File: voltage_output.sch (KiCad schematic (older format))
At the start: 29 parts, among them Q1 Q_NPN_BEC

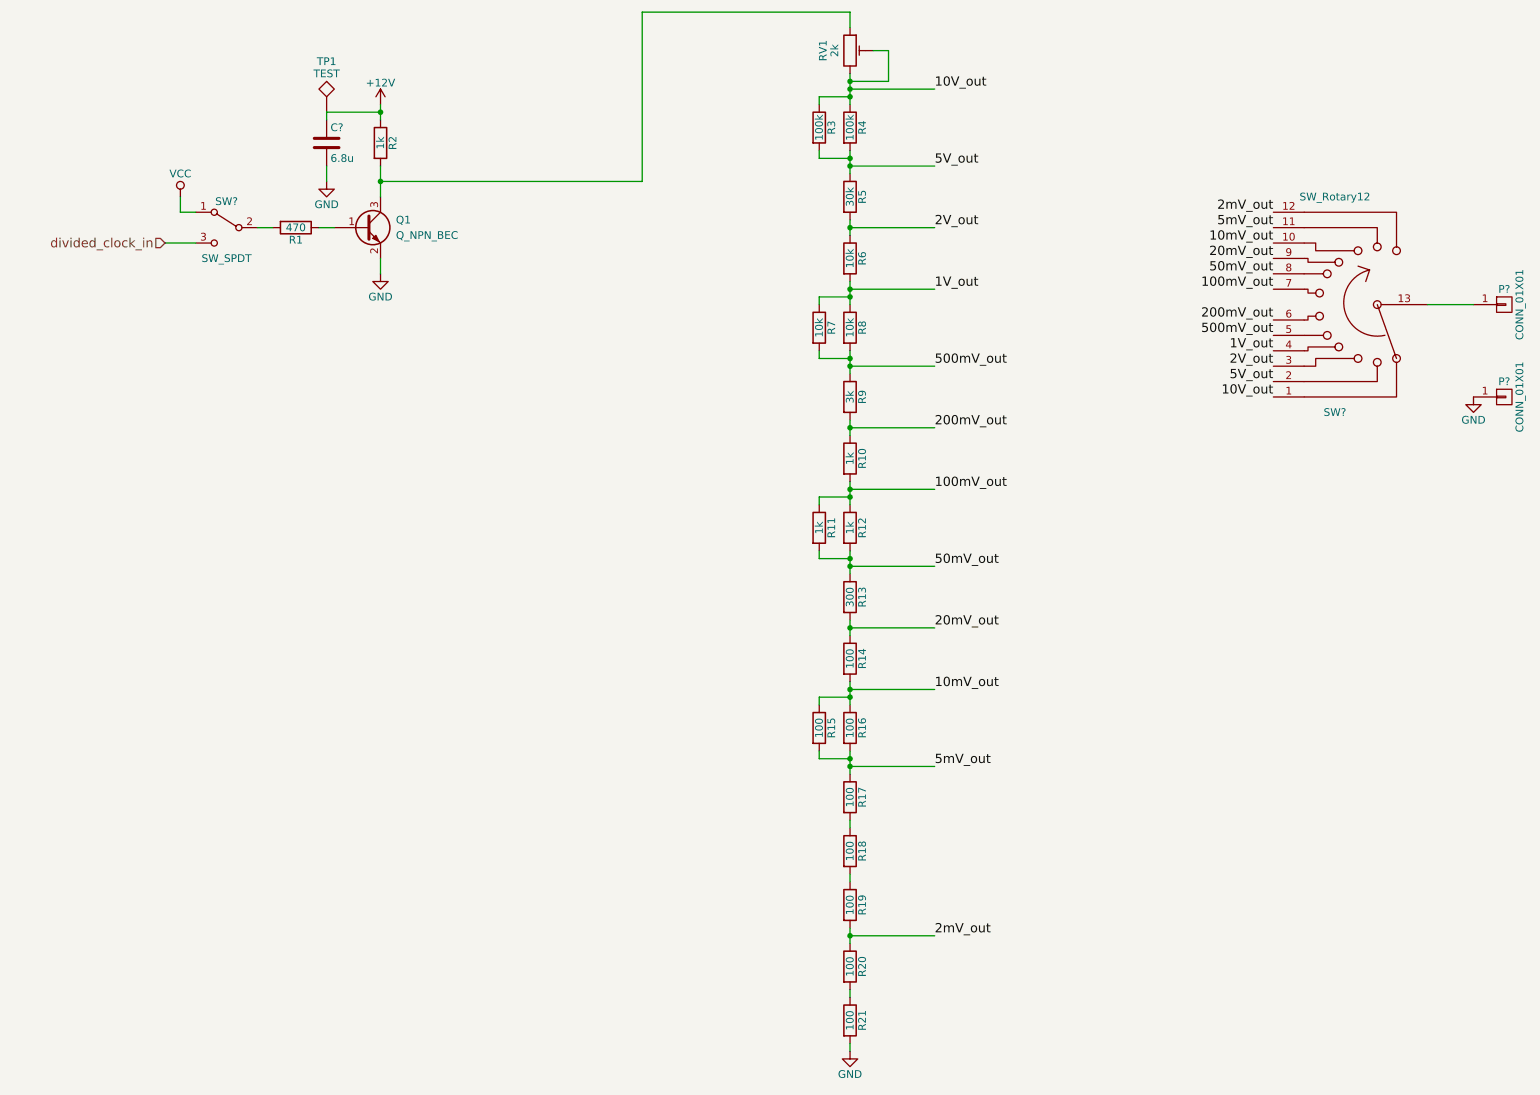
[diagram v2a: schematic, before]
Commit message: R2 PCB rotary switches closer to middle of board
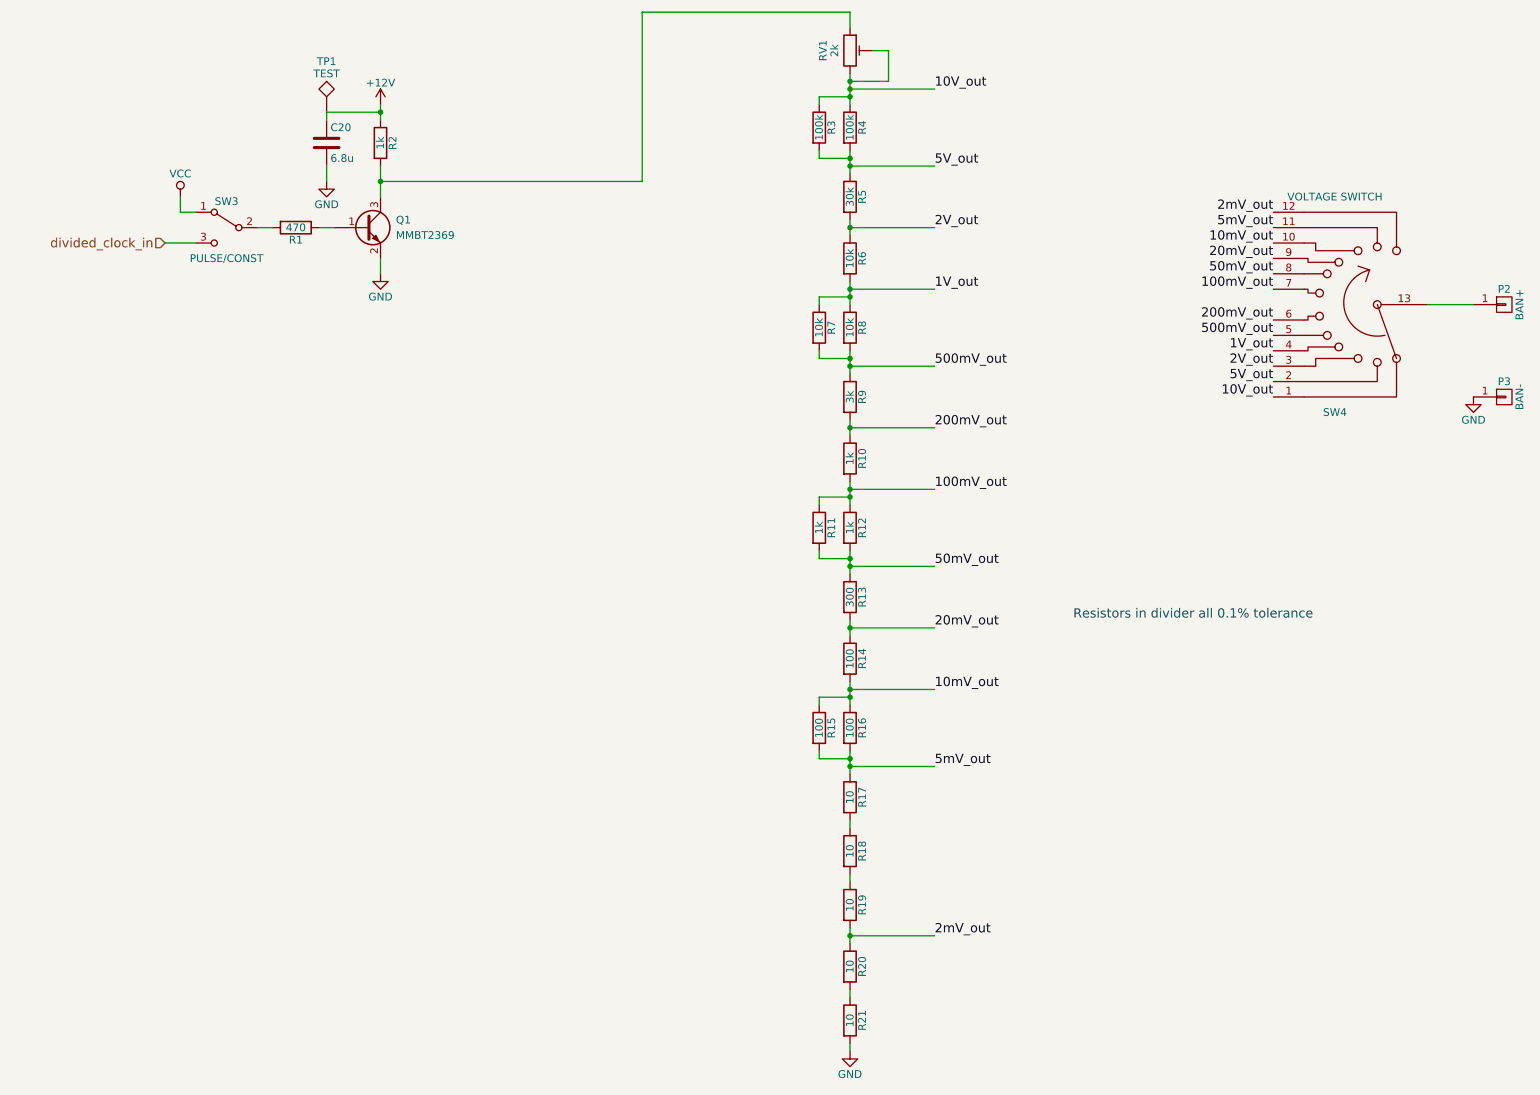
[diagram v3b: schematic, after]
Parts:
- P2: renamed from P?; value CONN_01X01 -> BAN+
- P3: renamed from P?; value CONN_01X01 -> BAN-
- Q1: value Q_NPN_BEC -> MMBT2369; Distributor (none) -> Mouser; Distributor PN (none) -> 863-MMBT2369ALT1G; Manufacturer (none) -> ON Semiconductor; Manufacturer PN (none) -> MMBT2369ALT1G; URL (none) -> http://www.mouser.com/Search/ProductDetail.aspx?R=MMBT2369A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; Unit Price (none) -> 0.19
- R17, R18, R19, R20, R21: value 100 -> 10
- RV1: Distributor (none) -> Mouser; Distributor PN (none) -> 652-3362P-1-202LF; Manufacturer (none) -> Bourns; Manufacturer PN (none) -> 3362P-1-202LF; URL (none) -> http://www.mouser.com/Search/ProductDetail.aspx?R=3362P-1-2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; Unit Price (none) -> 1.02
- SW3: renamed from SW?; value SW_SPDT -> PULSE/CONST; Distributor (none) -> Mouser; Distributor PN (none) -> 633-M201203; Manufacturer (none) -> NKK; Manufacturer PN (none) -> M2012SS1W03; URL (none) -> http://www.mouser.com/Search/ProductDetail.aspx?R=M2012SS1W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; Unit Price (none) -> 2.86
- SW4: renamed from SW?; value SW_Rotary12 -> VOLTAGE SWITCH; Distributor (none) -> Mouser; Distributor PN (none) -> 633-MRK112A; Manufacturer (none) -> NKK; Manufacturer PN (none) -> MRK112-A; URL (none) -> http://www.mouser.com/Search/ProductDetail.aspx?R=MRK112-Av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; Unit Price (none) -> 11.80
- gave numbers to parts that had none: 1
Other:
- note added: "Resistors in divider all 0.1% tolerance"
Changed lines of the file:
@@
 encoding utf-8
 Sheet 5 6
-Title ""
+Title "calbox voltage output"
 Date ""
 Rev ""
@@
 $EndDescr
 $Comp
-L CONN_01X01 P?
+L CONN_01X01 P2
 U 1 1 58C454A6
 P 10000 2500
-F 0 "P?" H 10000 2600 50  0000 C CNN
-F 1 "CONN_01X01" V 10100 2500 50  0000 C CNN
+F 0 "P2" H 10000 2600 50  0000 C CNN
+F 1 "BAN+" V 10100 2500 50  0000 C CNN
 F 2 "Pin_Headers:Pin_Header_Straight_1x01" H 10000 2500 50  0001 C CNN
 F 3 "" H 10000 2500 50  0000 C CNN
@@
 $EndComp
 $Comp
-L CONN_01X01 P?
+L CONN_01X01 P3
 U 1 1 58C454F0
 P 10000 3100
-F 0 "P?" H 10000 3200 50  0000 C CNN
-F 1 "CONN_01X01" V 10100 3100 50  0000 C CNN
+F 0 "P3" H 10000 3200 50  0000 C CNN
+F 1 "BAN-" V 10100 3100 50  0000 C CNN
 F 2 "Pin_Headers:Pin_Header_Straight_1x01" H 10000 3100 50  0001 C CNN
 F 3 "" H 10000 3100 50  0000 C CNN
@@
 P 5750 5700
 F 0 "R17" V 5830 5700 50  0000 C CNN
-F 1 "100" V 5750 5700 50  0000 C CNN
+F 1 "10" V 5750 5700 50  0000 C CNN
 F 2 "Resistors_SMD:R_0805_HandSoldering" V 5680 5700 50  0001 C CNN
 F 3 "" H 5750 5700 50  0000 C CNN
@@
 P 5750 7150
 F 0 "R21" V 5830 7150 50  0000 C CNN
-F 1 "100" V 5750 7150 50  0000 C CNN
+F 1 "10" V 5750 7150 50  0000 C CNN
 F 2 "Resistors_SMD:R_0805_HandSoldering" V 5680 7150 50  0001 C CNN
 F 3 "" H 5750 7150 50  0000 C CNN
@@
 $EndComp
 $Comp
-L GND #PWR67
+L GND #PWR063
 U 1 1 58C45C04
 P 5750 7350
-F 0 "#PWR67" H 5750 7100 50  0001 C CNN
+F 0 "#PWR063" H 5750 7100 50  0001 C CNN
 F 1 "GND" H 5750 7200 50  0000 C CNN
 F 2 "" H 5750 7350 50  0000 C CNN
@@
 $EndComp
 $Comp
-L GND #PWR68
+L GND #PWR064
 U 1 1 58C4A090
 P 9800 3100
-F 0 "#PWR68" H 9800 2850 50  0001 C CNN
+F 0 "#PWR064" H 9800 2850 50  0001 C CNN
 F 1 "GND" H 9800 2950 50  0000 C CNN
 F 2 "" H 9800 3100 50  0000 C CNN
@@
 divided_clock_in
 $Comp
-L SW_SPDT SW?
+L SW_SPDT SW3
 U 1 1 58C4AE53
 P 1700 2000
-F 0 "SW?" H 1700 2170 50  0000 C CNN
-F 1 "SW_SPDT" H 1700 1800 50  0000 C CNN
+F 0 "SW3" H 1700 2170 50  0000 C CNN
+F 1 "PULSE/CONST" H 1700 1800 50  0000 C CNN
 F 2 "calbox:SW_SPDT_NKK_M201xxxx03" H 1700 2000 50  0001 C CNN
-F 3 "" H 1700 2000 50  0000 C CNN
+F 3 "http://www.mouser.com/ds/2/295/MtogglesBushing-31423.pdf" H 1700 2000 50  0001 C CNN
+F 4 "NKK" H 1700 2000 60  0001 C CNN "Manufacturer"
+F 5 "M2012SS1W03" H 1700 2000 60  0001 C CNN "Manufacturer PN"
+F 6 "Mouser" H 1700 2000 60  0001 C CNN "Distributor"
+F 7 "633-M201203" H 1700 2000 60  0001 C CNN "Distributor PN"
+F 8 "http://www.mouser.com/Search/ProductDetail.aspx?R=M2012SS1W03virtualkey63300000virtualkey633-M201203" H 1700 2000 60  0001 C CNN "URL"
+F 9 "2.86" H 1700 2000 60  0001 C CNN "Unit Price"
 	1    1700 2000
 	-1   0    0    -1
@@
 F 1 "2k" V 5650 850 50  0000 C CNN
 F 2 "calbox:Potentiometer_Bourns_3362_ScrewUp" H 5750 850 50  0001 C CNN
-F 3 "" H 5750 850 50  0000 C CNN
+F 3 "http://www.mouser.com/ds/2/54/362-776956.pdf" H 5750 850 50  0001 C CNN
+F 4 "Bourns" V 5750 850 60  0001 C CNN "Manufacturer"
+F 5 "3362P-1-202LF" V 5750 850 60  0001 C CNN "Manufacturer PN"
+F 6 "Mouser" V 5750 850 60  0001 C CNN "Distributor"
+F 7 "652-3362P-1-202LF" V 5750 850 60  0001 C CNN "Distributor PN"
+F 8 "http://www.mouser.com/Search/ProductDetail.aspx?R=3362P-1-202LFvirtualkey65210000virtualkey652-3362P-1-202LF" V 5750 850 60  0001 C CNN "URL"
+F 9 "1.02" V 5750 850 60  0001 C CNN "Unit Price"
 	1    5750 850
 	1    0    0    -1
 $EndComp
 $Comp
-L SW_Rotary12 SW?
+L SW_Rotary12 SW4
 U 1 1 58C77F96
 P 8900 2500
-F 0 "SW?" H 8900 3200 50  0000 C CNN
-F 1 "SW_Rotary12" H 8900 1800 50  0000 C CNN
+F 0 "SW4" H 8900 3200 50  0000 C CNN
+F 1 "VOLTAGE SWITCH" H 8900 1800 50  0000 C CNN
 F 2 "calbox:SW_ROTARY_SP12T_MRK112" H 8700 3200 50  0001 C CNN
-F 3 "" H 8700 3200 50  0001 C CNN
+F 3 "http://www.mouser.com/ds/2/295/MRlogicLevel-9701.pdf" H 8700 3200 50  0001 C CNN
+F 4 "NKK" H 8900 2500 60  0001 C CNN "Manufacturer"
+F 5 "MRK112-A" H 8900 2500 60  0001 C CNN "Manufacturer PN"
+F 6 "Mouser" H 8900 2500 60  0001 C CNN "Distributor"
+F 7 "633-MRK112A" H 8900 2500 60  0001 C CNN "Distributor PN"
+F 8 "http://www.mouser.com/Search/ProductDetail.aspx?R=MRK112-Avirtualkey63300000virtualkey633-MRK112A" H 8900 2500 60  0001 C CNN "URL"
+F 9 "11.80" H 8900 2500 60  0001 C CNN "Unit Price"
 	1    8900 2500
 	-1   0    0    1
@@
 P 2600 2000
 F 0 "Q1" H 2800 2050 50  0000 L CNN
-F 1 "Q_NPN_BEC" H 2800 1950 50  0000 L CNN
+F 1 "MMBT2369" H 2800 1950 50  0000 L CNN
 F 2 "TO_SOT_Packages_SMD:SOT-23_Handsoldering" H 2800 2100 50  0001 C CNN
-F 3 "" H 2600 2000 50  0000 C CNN
+F 3 "http://www.mouser.com/ds/2/308/MMBT2369LT1-D-108591.pdf" H 2600 2000 50  0001 C CNN
+F 4 "ON Semiconductor" H 2600 2000 60  0001 C CNN "Manufacturer"
+F 5 "MMBT2369ALT1G" H 2600 2000 60  0001 C CNN "Manufacturer PN"
+F 6 "Mouser" H 2600 2000 60  0001 C CNN "Distributor"
+F 7 "863-MMBT2369ALT1G" H 2600 2000 60  0001 C CNN "Distributor PN"
+F 8 "http://www.mouser.com/Search/ProductDetail.aspx?R=MMBT2369ALT1Gvirtualkey58410000virtualkey863-MMBT2369ALT1G" H 2600 2000 60  0001 C CNN "URL"
+F 9 "0.19" H 2600 2000 60  0001 C CNN "Unit Price"
 	1    2600 2000
 	1    0    0    -1
@@
 $EndComp
 $Comp
-L +12V #PWR65
+L +12V #PWR065
 U 1 1 58C7B681
 P 2700 1200
-F 0 "#PWR65" H 2700 1050 50  0001 C CNN
+F 0 "#PWR065" H 2700 1050 50  0001 C CNN
 F 1 "+12V" H 2700 1340 50  0000 C CNN
 F 2 "" H 2700 1200 50  0000 C CNN
@@
 $EndComp
 $Comp
-L GND #PWR66
+L GND #PWR066
 U 1 1 58C7B717
 P 2700 2300
-F 0 "#PWR66" H 2700 2050 50  0001 C CNN
+F 0 "#PWR066" H 2700 2050 50  0001 C CNN
 F 1 "GND" H 2700 2150 50  0000 C CNN
 F 2 "" H 2700 2300 50  0000 C CNN
@@
 $EndComp
 $Comp
-L VCC #PWR63
+L VCC #PWR067
 U 1 1 58C7CD5D
 P 1400 1800
-F 0 "#PWR63" H 1400 1650 50  0001 C CNN
+F 0 "#PWR067" H 1400 1650 50  0001 C CNN
 F 1 "VCC" H 1400 1950 50  0000 C CNN
 F 2 "" H 1400 1800 50  0000 C CNN
@@
 $EndComp
 $Comp
-L C C?
+L C C20
 U 1 1 58C9DD95
 P 2350 1450
-F 0 "C?" H 2375 1550 50  0000 L CNN
+F 0 "C20" H 2375 1550 50  0000 L CNN
 F 1 "6.8u" H 2375 1350 50  0000 L CNN
 F 2 "Capacitors_SMD:C_0805_HandSoldering" H 2388 1300 50  0001 C CNN
@@
 $EndComp
 $Comp
-L GND #PWR64
+L GND #PWR068
 U 1 1 58C9DDF5
 P 2350 1700
-F 0 "#PWR64" H 2350 1450 50  0001 C CNN
+F 0 "#PWR068" H 2350 1450 50  0001 C CNN
 F 1 "GND" H 2350 1550 50  0000 C CNN
 F 2 "" H 2350 1700 50  0000 C CNN
@@
 P 5750 6050
 F 0 "R18" V 5830 6050 50  0000 C CNN
-F 1 "100" V 5750 6050 50  0000 C CNN
+F 1 "10" V 5750 6050 50  0000 C CNN
 F 2 "Resistors_SMD:R_0805_HandSoldering" V 5680 6050 50  0001 C CNN
 F 3 "" H 5750 6050 50  0000 C CNN
@@
 P 5750 6400
 F 0 "R19" V 5830 6400 50  0000 C CNN
-F 1 "100" V 5750 6400 50  0000 C CNN
+F 1 "10" V 5750 6400 50  0000 C CNN
 F 2 "Resistors_SMD:R_0805_HandSoldering" V 5680 6400 50  0001 C CNN
 F 3 "" H 5750 6400 50  0000 C CNN
@@
 P 5750 6800
 F 0 "R20" V 5830 6800 50  0000 C CNN
-F 1 "100" V 5750 6800 50  0000 C CNN
+F 1 "10" V 5750 6800 50  0000 C CNN
 F 2 "Resistors_SMD:R_0805_HandSoldering" V 5680 6800 50  0001 C CNN
 F 3 "" H 5750 6800 50  0000 C CNN
@@
 	1400 1900 1500 1900
 Wire Wire Line
-	5750 1000 5750 1050
-Wire Wire Line
-	5750 1050 5750 1100
-Wire Wire Line
-	5750 1100 5750 1150
-Wire Wire Line
-	5750 1150 5750 1200
+	5750 1000 5750 1200
 Wire Wire Line
 	5750 1050 6000 1050
@@
 	5750 7300 5750 7350
 Wire Wire Line
-	5750 5400 5750 5450
-Wire Wire Line
-	5750 5450 5750 5500
-Wire Wire Line
-	5750 5500 5750 5550
-Wire Wire Line
-	5750 4950 5750 5000
-Wire Wire Line
-	5750 5000 5750 5050
-Wire Wire Line
-	5750 5050 5750 5100
-Wire Wire Line
-	5750 4550 5750 4600
-Wire Wire Line
-	5750 4600 5750 4650
+	5750 5400 5750 5550
+Wire Wire Line
+	5750 4950 5750 5100
+Wire Wire Line
+	5750 4550 5750 4650
 Wire Wire Line
 	6300 6600 5750 6600
@@
 Connection ~ 5750 4600
 Wire Wire Line
-	5750 3650 5750 3700
-Wire Wire Line
-	5750 3700 5750 3750
-Wire Wire Line
-	5750 3750 5750 3800
-Wire Wire Line
-	5750 4100 5750 4150
-Wire Wire Line
-	5750 4150 5750 4200
-Wire Wire Line
-	5750 4200 5750 4250
+	5750 3650 5750 3800
+Wire Wire Line
+	5750 4100 5750 4250
 Wire Wire Line
 	5750 4200 6300 4200
@@
 Connection ~ 5750 3700
 Wire Wire Line
-	5750 3250 5750 3300
-Wire Wire Line
-	5750 3300 5750 3350
+	5750 3250 5750 3350
 Wire Wire Line
 	6300 3300 5750 3300
 Connection ~ 5750 3300
 Wire Wire Line
-	5750 2800 5750 2850
-Wire Wire Line
-	5750 2850 5750 2900
-Wire Wire Line
-	5750 2900 5750 2950
+	5750 2800 5750 2950
 Wire Wire Line
 	6300 2900 5750 2900
 Connection ~ 5750 2900
 Wire Wire Line
-	5750 2350 5750 2400
-Wire Wire Line
-	5750 2400 5750 2450
-Wire Wire Line
-	5750 2450 5750 2500
+	5750 2350 5750 2500
 Wire Wire Line
 	5750 2400 6300 2400
 Connection ~ 5750 2400
 Wire Wire Line
-	5750 1950 5750 2000
-Wire Wire Line
-	5750 2000 5750 2050
+	5750 1950 5750 2050
 Wire Wire Line
 	6300 2000 5750 2000
 Connection ~ 5750 2000
 Wire Wire Line
-	5750 1500 5750 1550
-Wire Wire Line
-	5750 1550 5750 1600
-Wire Wire Line
-	5750 1600 5750 1650
+	5750 1500 5750 1650
 Wire Wire Line
 	6300 1600 5750 1600
@@
 	2400 2000 2300 2000
 Wire Wire Line
-	2700 1600 2700 1700
-Wire Wire Line
-	2700 1700 2700 1800
-Wire Wire Line
-	2700 1200 2700 1250
-Wire Wire Line
-	2700 1250 2700 1300
+	2700 1600 2700 1800
+Wire Wire Line
+	2700 1200 2700 1300
 Wire Wire Line
 	2700 2300 2700 2200
@@
 	5750 6250 5750 6200
 Wire Wire Line
-	5750 6550 5750 6600
-Wire Wire Line
-	5750 6600 5750 6650
+	5750 6550 5750 6650
 Connection ~ 5750 6600
 Wire Wire Line
 	5750 6950 5750 7000
+Text Notes 7200 4550 0    60   ~ 0
+Resistors in divider all 0.1% tolerance
 $EndSCHEMATC

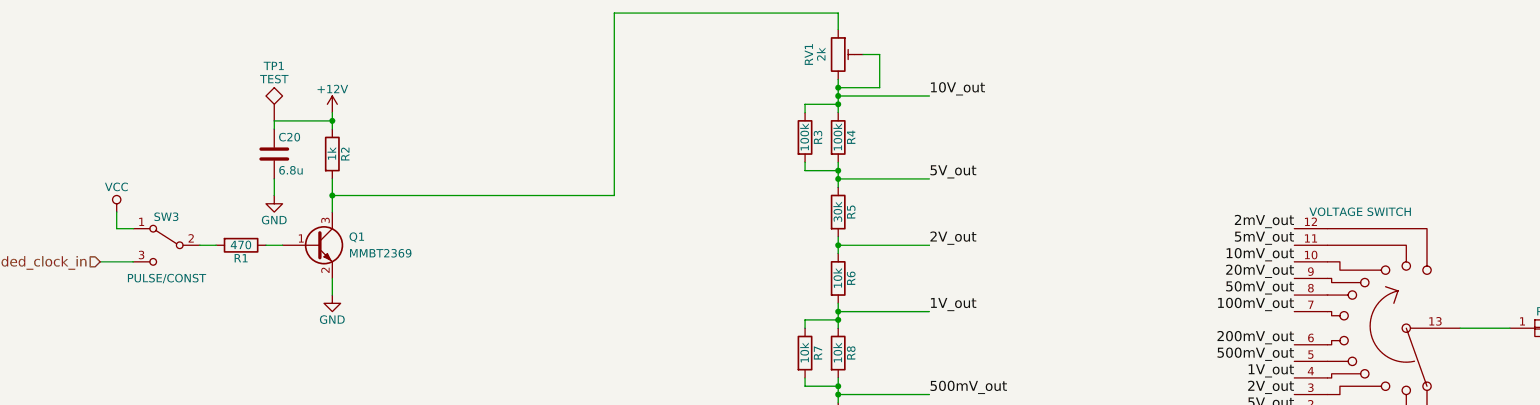
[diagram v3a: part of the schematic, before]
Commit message: update switch models in library, rotate final clock division switch
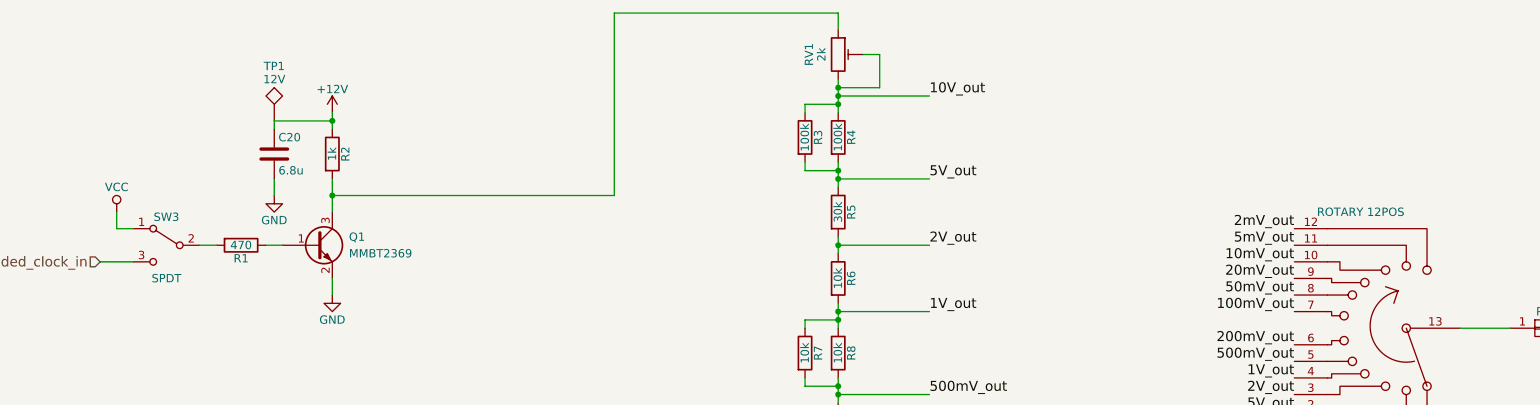
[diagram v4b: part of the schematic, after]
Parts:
- SW3: value PULSE/CONST -> SPDT
- SW4: value VOLTAGE SWITCH -> ROTARY 12POS
- TP1: value TEST -> 12V
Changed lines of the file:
@@
 P 1700 2000
 F 0 "SW3" H 1700 2170 50  0000 C CNN
-F 1 "PULSE/CONST" H 1700 1800 50  0000 C CNN
+F 1 "SPDT" H 1700 1800 50  0000 C CNN
 F 2 "calbox:SW_SPDT_NKK_M201xxxx03" H 1700 2000 50  0001 C CNN
 F 3 "http://www.mouser.com/ds/2/295/MtogglesBushing-31423.pdf" H 1700 2000 50  0001 C CNN
@@
 P 8900 2500
 F 0 "SW4" H 8900 3200 50  0000 C CNN
-F 1 "VOLTAGE SWITCH" H 8900 1800 50  0000 C CNN
+F 1 "ROTARY 12POS" H 8900 1800 50  0000 C CNN
 F 2 "calbox:SW_ROTARY_SP12T_MRK112" H 8700 3200 50  0001 C CNN
 F 3 "http://www.mouser.com/ds/2/295/MRlogicLevel-9701.pdf" H 8700 3200 50  0001 C CNN
@@
 P 2350 1250
 F 0 "TP1" H 2350 1550 50  0000 C BNN
-F 1 "TEST" H 2350 1500 50  0000 C CNN
+F 1 "12V" H 2350 1500 50  0000 C CNN
 F 2 "Measurement_Points:Measurement_Point_Square-TH_Big" H 2350 1250 50  0001 C CNN
 F 3 "" H 2350 1250 50  0000 C CNN
